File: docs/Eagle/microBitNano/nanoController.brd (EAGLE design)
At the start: 63.6 x 80 mm, 12 parts, among them J2 MTXNRX, J3 IR RX, J4 IR TX, J8 MRXNTX

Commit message: crossover
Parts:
- added J10, J11, J12, J13, J14, J15, J16, J26, J27, J9: (no value), SparkFun-Connectors:1X01
- added J17, J18, J19, J20, J21, J22, J23, J24: IR RX, SparkFun-Connectors:1X03
- added J25: (no value), SparkFun-Connectors:1X11
- added J28: MTXNRX, SparkFun-Connectors:1X02
- added LED3: (no value), SparkFun-Connectors:1X04_LONGPADS
- added R1, R2, R3: (no value), resistor-power:HPS58
- moved J4 16.9 mm to (35.6, 69.8)
- moved J2 11.5 mm to (50.8, 41.9)
- moved J8 10.2 mm to (50.8, 34.3)
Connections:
- new net 3.3V: J10.1, J28.2, J5.P$1
- new net 7.4V: J14.1, J15.1, J9.1
- new net D11: JP5.14
- new net D12: JP5.15
- new net N$1: LED3.4, R1.2
- new net N$2: LED3.3, R2.2
- new net N$3: LED3.1, R3.1
- net D2: now also J26.1
- net D4: now also R1.1
- net D7: now also R2.1
- net D8: now also R3.2
- net GND: now also J11.1, J12.1, J13.1, J16.1, J17.1, J18.1, J19.1, J20.1, J21.1, J22.1, J23.1, J24.1, J27.1
- net M0: now also J17.3
- net M1: now also J18.3
- net M10: now also J25.3
- net M11: now also J25.4
- net M12: now also J25.5
- net M13: now also J25.6
- net M14: now also J25.7
- net M15: now also J25.8
- net M16: now also J25.9; no longer JP5.15
- net M19: now also J25.10
- net M2: now also J19.3
- net M20: now also J25.11
- net M3: now also J20.3
- net M4: now also J21.3
- net M5: now also J22.3
- net M6: now also J23.3
- net M7: now also J24.3
- net M8: now also J25.1; no longer JP5.14
- net M9: now also J25.2
- net VCC: now also J17.2, J18.2, J19.2, J20.2, J21.2, J22.2, J23.2, J24.2, J28.1, LED3.2; no longer J5.P$1
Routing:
- net M16: track 124.4 -> 5.08 mm
- net 3.3V: track 0.00 -> 117.3 mm
- net M8: track 104.2 -> 21.0 mm
- net GND: track 137.2 -> 214.7 mm
- net M6: track 0.00 -> 48.7 mm
- net M7: track 0.00 -> 42.7 mm
- net D2: track 0.00 -> 41.1 mm
- net M4: track 0.00 -> 35.8 mm
- net M5: track 0.00 -> 35.7 mm, vias 0 -> 1
- net D8: track 0.00 -> 35.5 mm
- net M3: track 0.00 -> 30.0 mm
- net D7: track 0.00 -> 29.5 mm
- net D4: track 0.00 -> 27.4 mm
- net 7.4V: track 0.00 -> 27.0 mm
- net M2: track 0.00 -> 25.7 mm
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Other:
- board size 63.6 x 80 mm -> 67.4 x 79.9 mm
- board text added: "- + 0"
- board text added: "- + 1"
- board text added: "- + 2"
- board text added: "- + 3"
- board text added: "- + 4"
- board text added: "- + 5"
- board text added: "7.4"
- board text added: "D2"
- board text added: "GD3"
- board text added: "VGD17"
- board text added: "on/off"
- board text removed: "GD"
- board text removed: "VGD"

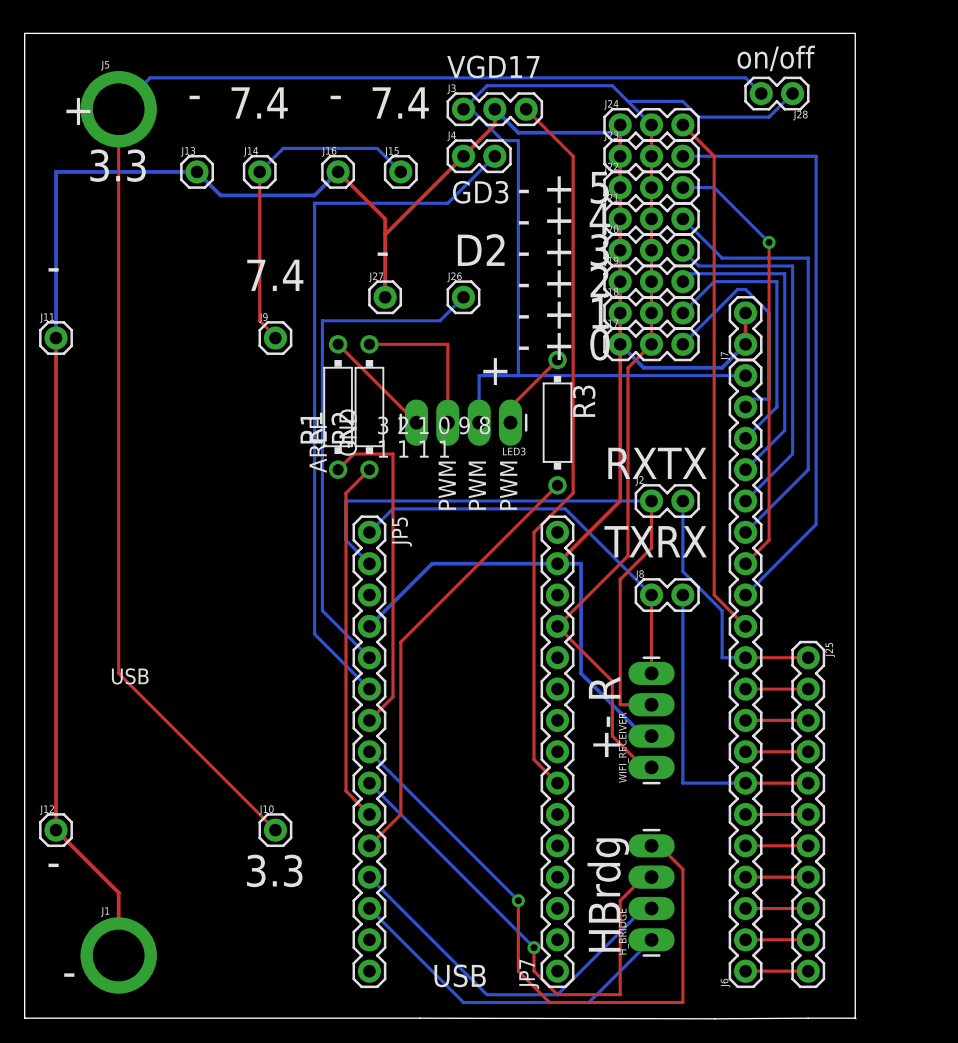
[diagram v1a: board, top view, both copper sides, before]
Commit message: Added spider/biped assembly
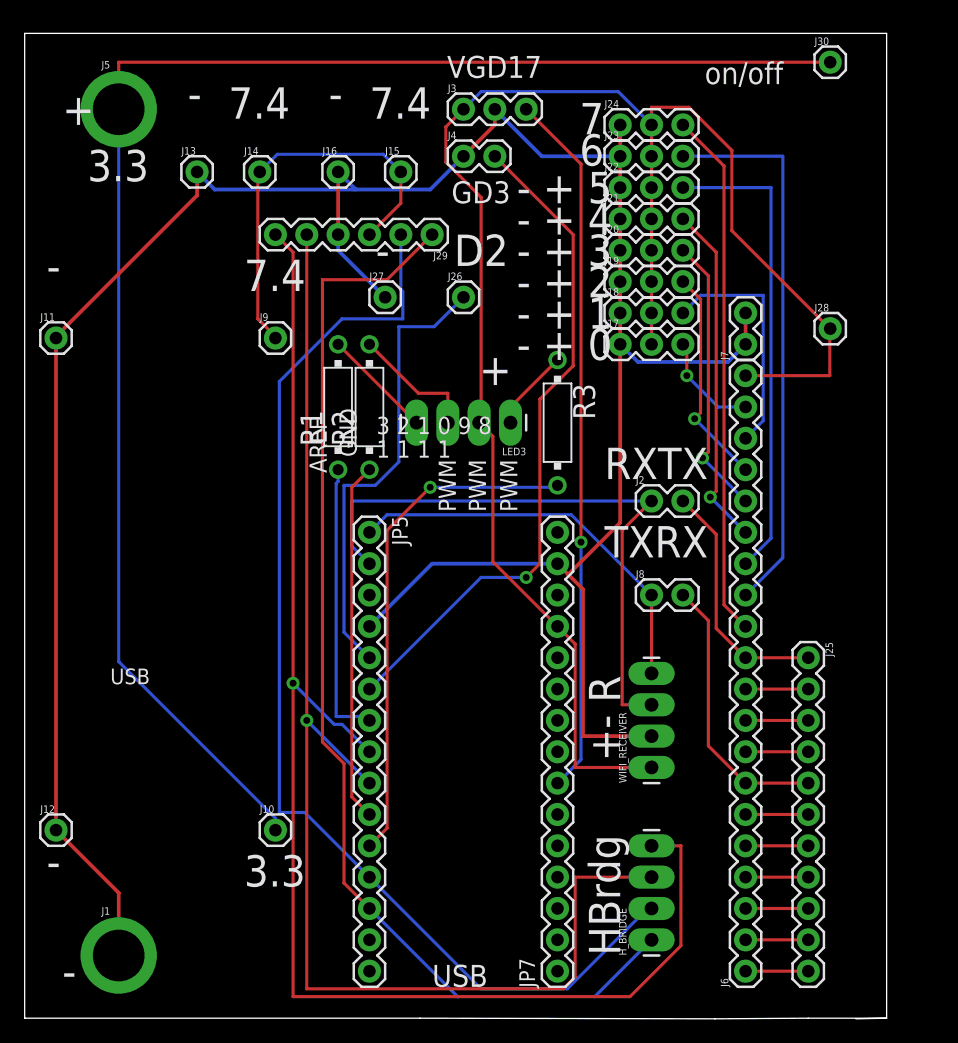
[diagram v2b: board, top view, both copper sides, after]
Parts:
- added J29: (no value), SparkFun-Connectors:1X06
- added J30: (no value), SparkFun-Connectors:1X01
- J28: value MTXNRX -> (none); device SparkFun-Connectors:1X02 -> SparkFun-Connectors:1X01
- moved J28 19.3 mm to (65.3, 55.9), turned to 0 degrees
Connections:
- net 3.3V: now also J30.1; no longer J28.2
- net 7.4V: now also J29.3
- net D10: now also J29.1
- net D5: now also J29.6
- net D6: now also J29.5
- net D9: now also J29.2
- net GND: now also J29.4
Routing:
- net D6: track 39.5 -> 104.7 mm
- net D5: track 51.3 -> 114.5 mm
- net D9: track 29.7 -> 92.7 mm
- net D10: track 28.1 -> 90.7 mm
- net M0: track 18.8 -> 8.49 mm, vias 0 -> 1
- net M2: track 25.7 -> 17.7 mm, vias 0 -> 1
- net M4: track 35.8 -> 27.9 mm, vias 0 -> 1
- net 3.3V: track 117.3 -> 125.1 mm
- net M3: track 30.0 -> 22.8 mm, vias 0 -> 1
- net D8: track 35.5 -> 41.5 mm, vias 0 -> 1
- net 7.4V: track 27.0 -> 32.9 mm
- net D4: track 27.4 -> 22.9 mm
- net D2: track 41.1 -> 37.2 mm
- net M6: track 48.7 -> 44.9 mm
- net VCC: track 140.7 -> 137.2 mm
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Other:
- board size 67.4 x 79.9 mm -> 69.8 x 79.9 mm
- board text added: "6"
- board text added: "7"

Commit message: hyo
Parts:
- added PROTECT-MICROBIT: 1N5817-B, diode:DO41-7.6
- added S1: (no value), switch-omron:B3F-10XX
- J3: value IR RX -> (none); device SparkFun-Connectors:1X03 -> SparkFun-Connectors:1X01
- J4: value IR TX -> (none); device SparkFun-Connectors:1X02 -> SparkFun-Connectors:1X01
- moved J3 35.8 mm to (71.1, 77.5)
- moved J4 22.9 mm to (57.1, 77.5)
- moved J26 3.78 mm to (38.4, 55.9)
- moved J27 3.59 mm to (31.8, 55.9)
- moved J28 1.27 mm to (64.0, 55.9)
- moved J30 1.27 mm to (64.0, 77.5)
- moved J29 1.27 mm to (33.0, 62.2)
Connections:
- new net BATT3.7V: J4.1, J5.P$1
- new net BATT7.4V: J14.1, J3.1
- new net N$4: JP7.12, PROTECT-MICROBIT.C
- net 3.3V: no longer J5.P$1
- net 7.4V: no longer J14.1
- net D17: no longer J3.3
- net D3: now also S1.2; no longer J4.2
- net GND: now also S1.4; no longer J3.2, J4.1
- net VCC: now also PROTECT-MICROBIT.A; no longer J3.1, JP7.12
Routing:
- net D17: track 57.2 -> 0.00 mm, vias 1 -> 0
- net BATT7.4V: track 0.00 -> 57.1 mm
- net BATT3.7V: track 0.00 -> 53.3 mm
- net D5: track 114.5 -> 154.4 mm, vias 1 -> 0
- net 3.3V: track 125.1 -> 105.9 mm
- net D3: track 54.8 -> 37.2 mm, vias 1 -> 0
- net M0: track 8.49 -> 26.1 mm, vias 1 -> 0
- net 7.4V: track 32.9 -> 18.0 mm
- net M2: track 17.7 -> 32.4 mm, vias 1 -> 0
- net M1: track 19.3 -> 29.7 mm
- net M5: track 38.5 -> 48.1 mm
- net VCC: track 137.2 -> 127.7 mm
- net M6: track 44.9 -> 37.7 mm
- net D8: track 41.5 -> 35.5 mm, vias 1 -> 0
- net D6: track 104.7 -> 109.7 mm
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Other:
- board size 69.8 x 79.9 mm -> 73.7 x 79.9 mm
- board text added: "3.3V"
- board text added: "7.4V"
- board text added: "BATTERY 7.4"
- board text added: "on/off switch"
- board text removed: "VGD17"
- board text removed: "on/off"
